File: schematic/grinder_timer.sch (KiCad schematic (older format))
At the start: 31 parts, among them J1 AVR-ISP-6, J2 SERIAL, K1 RELAY, P1 MOTOR, P2 ACTIVE, P3 NEUTRAL, Q1 NPN, T1 1P1S, U1 ATmega328PB-AU, U2 5V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

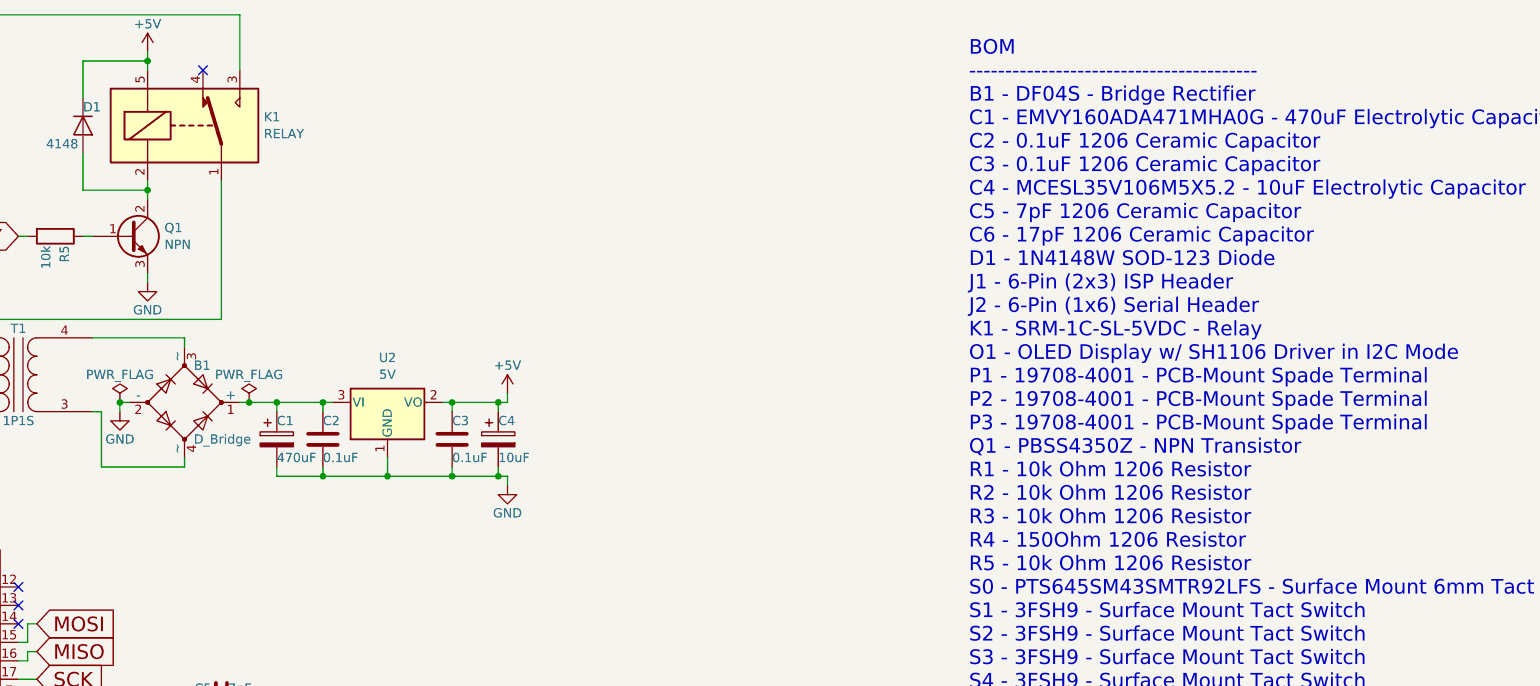
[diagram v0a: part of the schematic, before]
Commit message: Created custom footprints, assigned footprints to all symbols, began PCB layout.
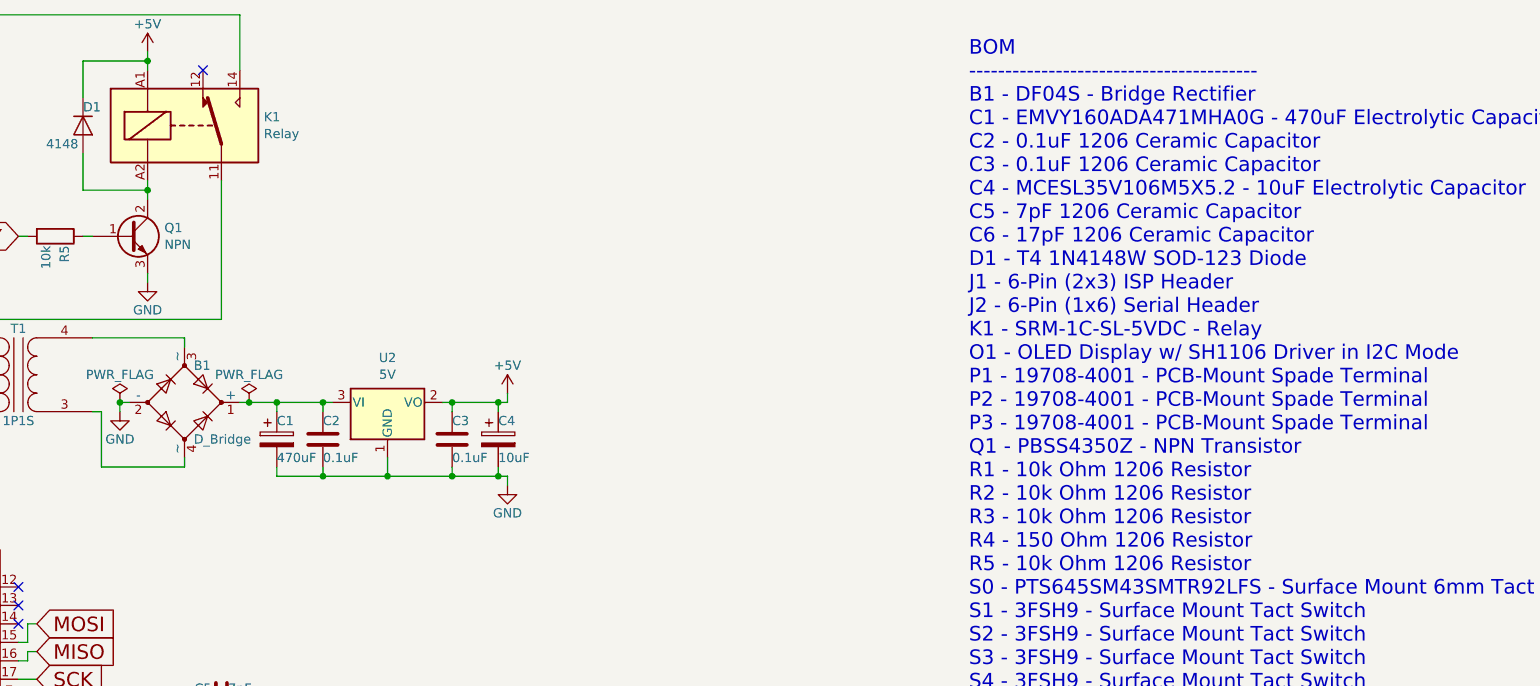
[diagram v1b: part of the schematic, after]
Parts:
- removed K1: RELAY, Relay_THT:Relay_SPDT_Omron-G5LE-1, symbol Relay:G5LE-1
- added K1: Relay, Relay_THT:Relay_SPDT_Finder_36.11, symbol Relay:FINDER-32.21-x000
- B1: footprint (none) -> Diode_SMD:Diode_Bridge_Vishay_DFS
- C1: footprint (none) -> Capacitor_SMD:C_Elec_8x10.2
- C2, C3, C5, C6: footprint (none) -> Capacitor_SMD:C_1206_3216Metric_Pad1.42x1.75mm_HandSolder
- C4: footprint (none) -> Capacitor_SMD:C_Elec_5x5.4
- D1: footprint (none) -> Diode_SMD:D_SOD-123
- J1: footprint (none) -> Connector_IDC:IDC-Header_2x03_P2.54mm_Vertical
- J2: footprint (none) -> Connector_PinHeader_2.54mm:PinHeader_1x06_P2.54mm_Horizontal
- O1: footprint (none) -> grinder_timer:oled
- P1, P2, P3: footprint (none) -> grinder_timer:pcb_tab
- Q1: footprint (none) -> Package_TO_SOT_SMD:SOT-223-3_TabPin2
- R1, R2, R3, R4, R5: footprint (none) -> Resistor_SMD:R_1206_3216Metric_Pad1.42x1.75mm_HandSolder
- S0: footprint (none) -> Button_Switch_SMD:SW_Push_1P1T_NO_6x6mm_H9.5mm
- S1, S2, S3, S4: footprint (none) -> grinder_timer:tact
- S5: footprint (none) -> grinder_timer:tact_led
- T1: footprint (none) -> grinder_timer:transformer
- Y1: footprint (none) -> Crystal:Crystal_SMD_Abracon_ABS25-4Pin_8.0x3.8mm
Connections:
- net +5V: now also K1.A1
- net at P2.1, T1.1 (AA): now also K1.11
- net at P1.1: now also K1.14
- net at D1.2 (A), Q1.2 (C): now also K1.A2
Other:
- note added: "BOM\n----------------------------------------\nB1 - DF04S - Bridge Rectifier\nC1 - EMVY160ADA471MHA0G - 470uF Electrolytic Capacitor\nC2 - 0.1uF 1206 Ceramic Capacitor\nC3 - 0.1uF 1206 Ceramic Capacitor\nC4 - MCESL35V106M5X5.2 - 10uF Electrolytic Capacitor\nC5 - 7pF 1206 Ceramic Capacitor\nC6 - 17pF 1206 Ceramic Capacitor\nD1 - T4 1N4148W SOD-123 Diode\nJ1 - 6-Pin (2x3) ISP Header\nJ2 - 6-Pin (1x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"
- note removed: "BOM\n----------------------------------------\nB1 - DF04S - Bridge Rectifier\nC1 - EMVY160ADA471MHA0G - 470uF Electrolytic Capacitor\nC2 - 0.1uF 1206 Ceramic Capacitor\nC3 - 0.1uF 1206 Ceramic Capacitor\nC4 - MCESL35V106M5X5.2 - 10uF Electrolytic Capacitor\nC5 - 7pF 1206 Ceramic Capacitor\nC6 - 17pF 1206 Ceramic Capacitor\nD1 - 1N4148W SOD-123 Diode\nJ1 - 6-Pin (2x3) ISP Header\nJ2 - 6-Pin (1x6) 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"

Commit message: Switched transformer.  Completed PCB layout.  Added silkscreen logos.
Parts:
- J2: footprint Connector_PinHeader_2.54mm:PinHeader_1x06_P2.54mm_Horizontal -> Connector_PinHeader_2.54mm:PinHeader_1x06_P2.54mm_Vertical
- T1: footprint grinder_timer:transformer -> grinder_timer:transformer_big
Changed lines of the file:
@@
 F 0 "T1" H 1900 3000 50  0000 C CNN
 F 1 "1P1S" H 1900 2500 50  0000 C CNN
-F 2 "grinder_timer:transformer" H 1900 2750 50  0001 C CNN
+F 2 "grinder_timer:transformer_big" H 1900 2750 50  0001 C CNN
 F 3 "~" H 1900 2750 50  0001 C CNN
 	1    1900 2750
@@
 F 0 "J2" H 5600 7100 50  0000 L CNN
 F 1 "SERIAL" H 5550 6400 50  0000 L CNN
-F 2 "Connector_PinHeader_2.54mm:PinHeader_1x06_P2.54mm_Horizontal" H 5650 6800 50  0001 C CNN
+F 2 "Connector_PinHeader_2.54mm:PinHeader_1x06_P2.54mm_Vertical" H 5650 6800 50  0001 C CNN
 F 3 "~" H 5650 6800 50  0001 C CNN
 	1    5650 6800
@@
 	2600 2250 2600 2200
 Text Notes 7050 5100 0    79   ~ 0
-BOM\n----------------------------------------\nB1 - DF04S - Bridge Rectifier\nC1 - EMVY160ADA471MHA0G - 470uF Electrolytic Capacitor\nC2 - 0.1uF 1206 Ceramic Capacitor\nC3 - 0.1uF 1206 Ceramic Capacitor\nC4 - MCESL35V106M5X5.2 - 10uF Electrolytic Capacitor\nC5 - 7pF 1206 Ceramic Capacitor\nC6 - 17pF 1206 Ceramic Capacitor\nD1 - T4 1N4148W SOD-123 Diode\nJ1 - 6-Pin (2x3) ISP Header\nJ2 - 6-Pin (1x6) Serial Header\nK1 - SRM-1C-SL-5VDC - Relay\nO1 - OLED Display w/ SH1106 Driver in I2C Mode\nP1 - 19708-4001 - PCB-Mount Spade Terminal\nP2 - 19708-4001 - PCB-Mount Spade Terminal\nP3 - 19708-4001 - PCB-Mount Spade Terminal\nQ1 - PBSS4350Z - NPN Transistor\nR1 - 10k Ohm 1206 Resistor\nR2 - 10k Ohm 1206 Resistor\nR3 - 10k Ohm 1206 Resistor\nR4 - 150 Ohm 1206 Resistor\nR5 - 10k Ohm 1206 Resistor\nS0 - PTS645SM43SMTR92LFS - Surface Mount 6mm Tact Switch\nS1 - 3FSH9 - Surface Mount Tact Switch\nS2 - 3FSH9 - Surface Mount Tact Switch\nS3 - 3FSH9 - Surface Mount Tact Switch\nS4 - 3FSH9 - Surface Mount Tact Switch\nS5 - 5GSH93561 - Surface Mount Tact Switch w/ LED\nT1 - 45001 - 6V Transformer\nU1 - ATMEGA328PB - Microcontroller\nU2 - MIC39100-5 - 5V LDO Linear Regulator\nY1 - FSRLF - 32.768kHz Crystal
+BOM\n----------------------------------------\nB1 - DF04S - Bridge Rectifier\nC1 - EMVY160ADA471MHA0G - 470uF Electrolytic Capacitor\nC2 - 0.1uF 1206 Ceramic Capacitor\nC3 - 0.1uF 1206 Ceramic Capacitor\nC4 - MCESL35V106M5X5.2 - 10uF Electrolytic Capacitor\nC5 - 7pF 1206 Ceramic Capacitor\nC6 - 17pF 1206 Ceramic Capacitor\nD1 - T4 1N4148W SOD-123 Diode\nJ1 - 6-Pin (2x3) ISP Header\nJ2 - 6-Pin (1x6) Serial Header\nK1 - SRM-1C-SL-5VDC - Relay\nO1 - OLED Display w/ SH1106 Driver in I2C Mode\nP1 - 19708-4001 - PCB-Mount Spade Terminal\nP2 - 19708-4001 - PCB-Mount Spade Terminal\nP3 - 19708-4001 - PCB-Mount Spade Terminal\nQ1 - PBSS4350Z - NPN Transistor\nR1 - 10k Ohm 1206 Resistor\nR2 - 10k Ohm 1206 Resistor\nR3 - 10k Ohm 1206 Resistor\nR4 - 150 Ohm 1206 Resistor\nR5 - 10k Ohm 1206 Resistor\nS0 - PTS645SM43SMTR92LFS - Surface Mount 6mm Tact Switch\nS1 - 3FSH9 - Surface Mount Tact Switch\nS2 - 3FSH9 - Surface Mount Tact Switch\nS3 - 3FSH9 - Surface Mount Tact Switch\nS4 - 3FSH9 - Surface Mount Tact Switch\nS5 - 5GSH93561 - Surface Mount Tact Switch w/ LED\nT1 - 44121 - 6V Transformer\nU1 - ATMEGA328PB - Microcontroller\nU2 - MIC39100-5 - 5V LDO Linear Regulator\nY1 - FSRLF - 32.768kHz Crystal
 $Comp
 L Relay:FINDER-32.21-x000 K1

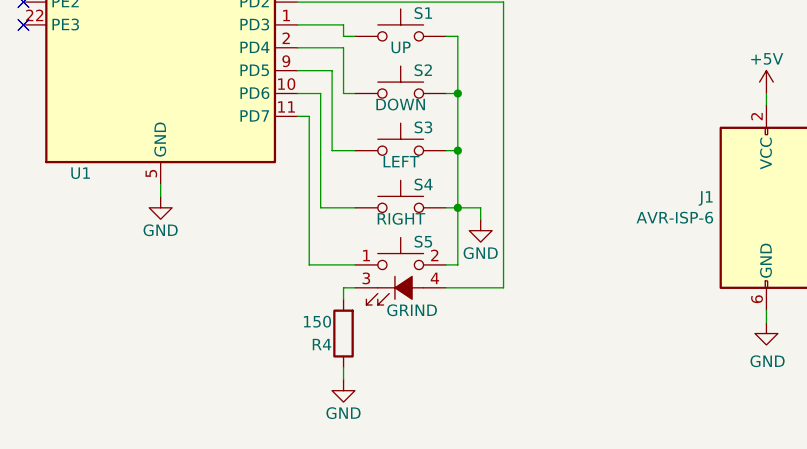
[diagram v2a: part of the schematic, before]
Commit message: Fixed let tact switch pinout.  Modified via sizes.
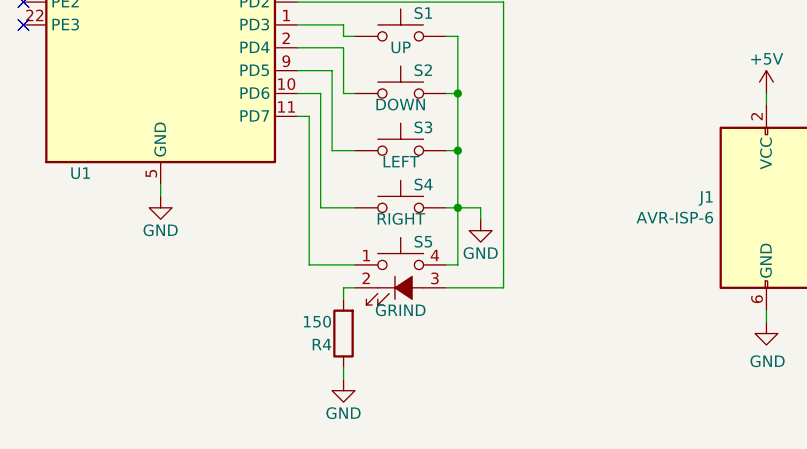
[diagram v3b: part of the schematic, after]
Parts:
- removed S5: GRIND, grinder_timer:tact_led, symbol Switch:SW_Push_LED
- added S5: GRIND, grinder_timer:tact_led, symbol Switch:SW_MEC_5G_LED
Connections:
- net GND: now also S5.4 (A)
- net at U1.11 (PD7): now also S5.1
- net at U1.32 (PD2): now also S5.3 (K)
- net at R4.2: now also S5.2
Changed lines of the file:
@@
 Wire Wire Line
 	3750 5550 3750 5600
-$Comp
-L Switch:SW_Push_LED S5
-U 1 1 5F2FE408
-P 2350 7050
-F 0 "S5" H 2450 7250 50  0000 C CNN
-F 1 "GRIND" H 2400 6950 50  0000 C CNN
-F 2 "grinder_timer:tact_led" H 2350 7350 50  0001 C CNN
-F 3 "~" H 2350 7350 50  0001 C CNN
-	1    2350 7050
-	1    0    0    -1
-$EndComp
 Wire Wire Line
 	2000 5650 1950 5650
@@
 	1    0    0    -1
 $EndComp
+$Comp
+L Switch:SW_MEC_5G_LED S5
+U 1 1 5F144751
+P 2350 7050
+F 0 "S5" H 2450 7250 50  0000 C CNN
+F 1 "GRIND" H 2350 6950 50  0000 C CNN
+F 2 "grinder_timer:tact_led" H 2350 7350 50  0001 C CNN
+F 3 "http://www.apem.com/int/index.php?controller=attachment&id_attachment=488" H 2350 7350 50  0001 C CNN
+	1    2350 7050
+	1    0    0    -1
+$EndComp
